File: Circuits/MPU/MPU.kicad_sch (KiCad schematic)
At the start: 12 parts, among them J1 5-1814400-1, J10 Conn_02x10_Odd_Even, J11 Conn_02x25_Odd_Even, J2 5-1814400-1, J3 DE9_Plug, J4 DE9_Plug, J5 0010085031, J6 DE9_Receptacle, J7 DE9_Receptacle, J8 Conn_02x05_Odd_Even, J9 Conn_02x13_Odd_Even, U1 ProASIC

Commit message: MXS interface
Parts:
- added J13: Pico-Lock-8, Connector_Molex:Molex_Pico-Lock_504050-0891_1x08-1MP_P1.50mm_Horizontal, symbol Connector_Generic:Conn_01x08
- J3, J4: value DE9_Plug -> MDM9_Plug
- J7: value DE9_Receptacle -> MDM9_Receptacle
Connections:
- net GND: now also J13.1 (Pin_1), J13.4 (Pin_4), J13.8 (Pin_8)
- new net Serial Interfaces/MXAD: J13.7 (Pin_7)
- new net Serial Interfaces/MXAS: J13.3 (Pin_3)
- new net Serial Interfaces/MXCLK: J13.5 (Pin_5)
- new net Serial Interfaces/MXDD: J13.6 (Pin_6)
- new net Serial Interfaces/MXDS: J13.2 (Pin_2)
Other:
- sheet Serial Interfaces ports: added MXAD, MXAS, MXCLK, MXDD, MXDS; removed none

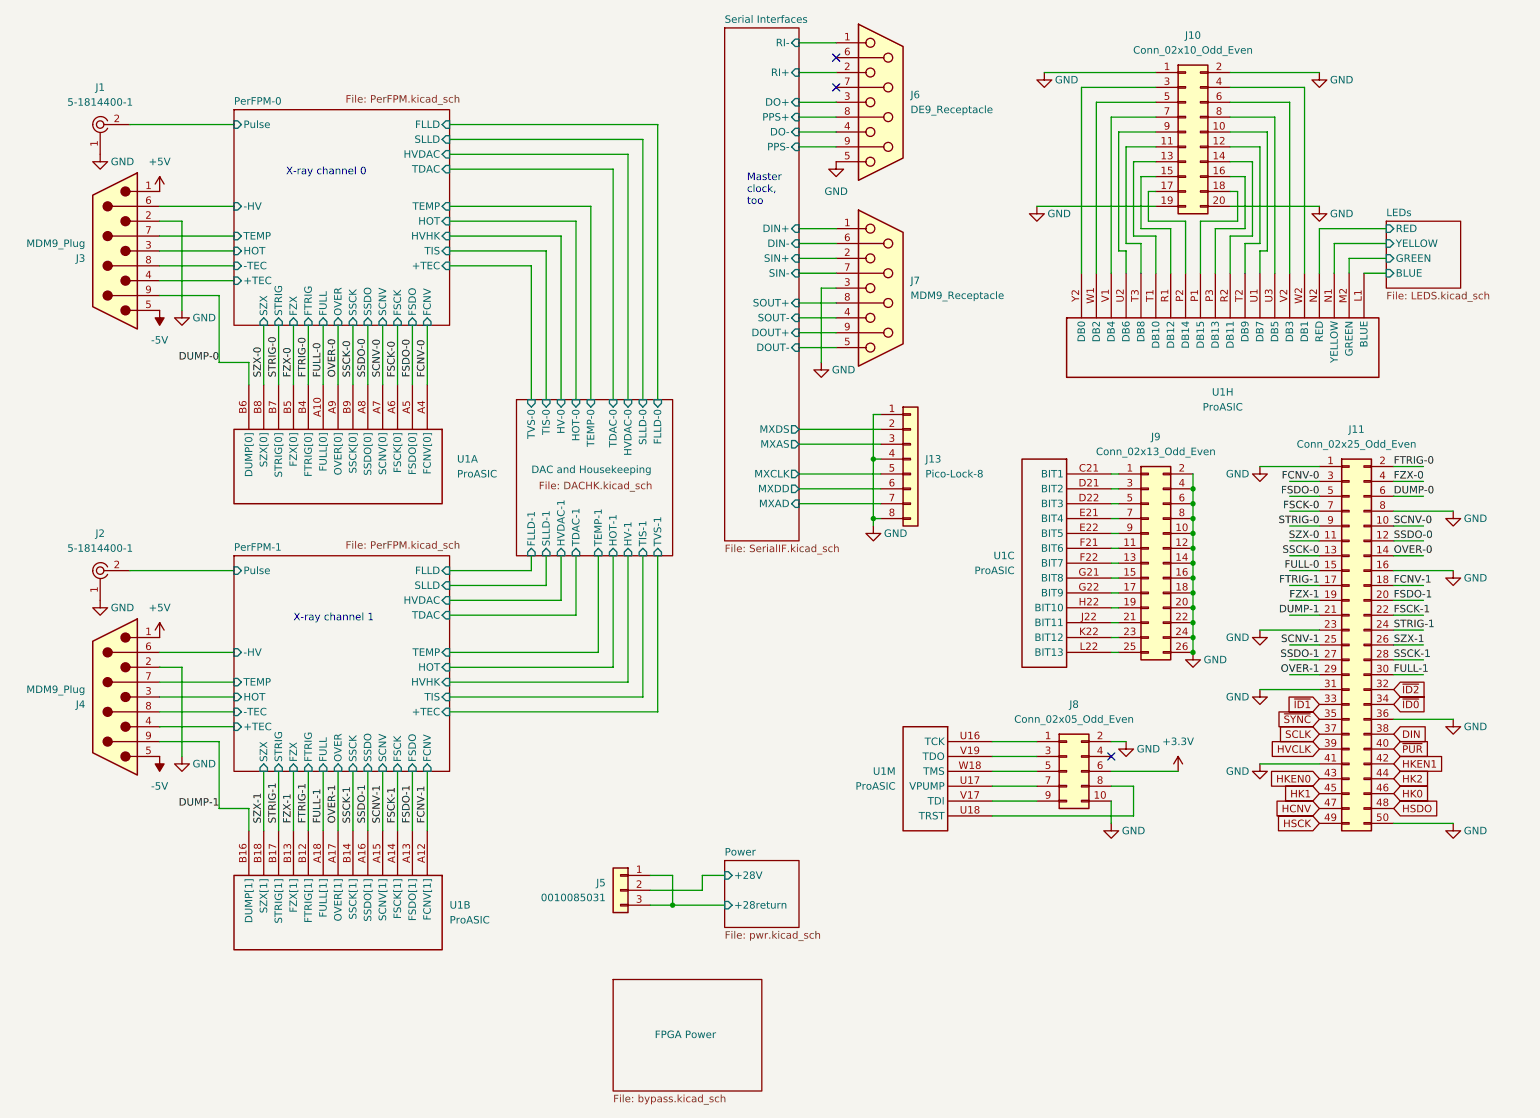
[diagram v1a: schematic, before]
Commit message: LVDS I/F for HV
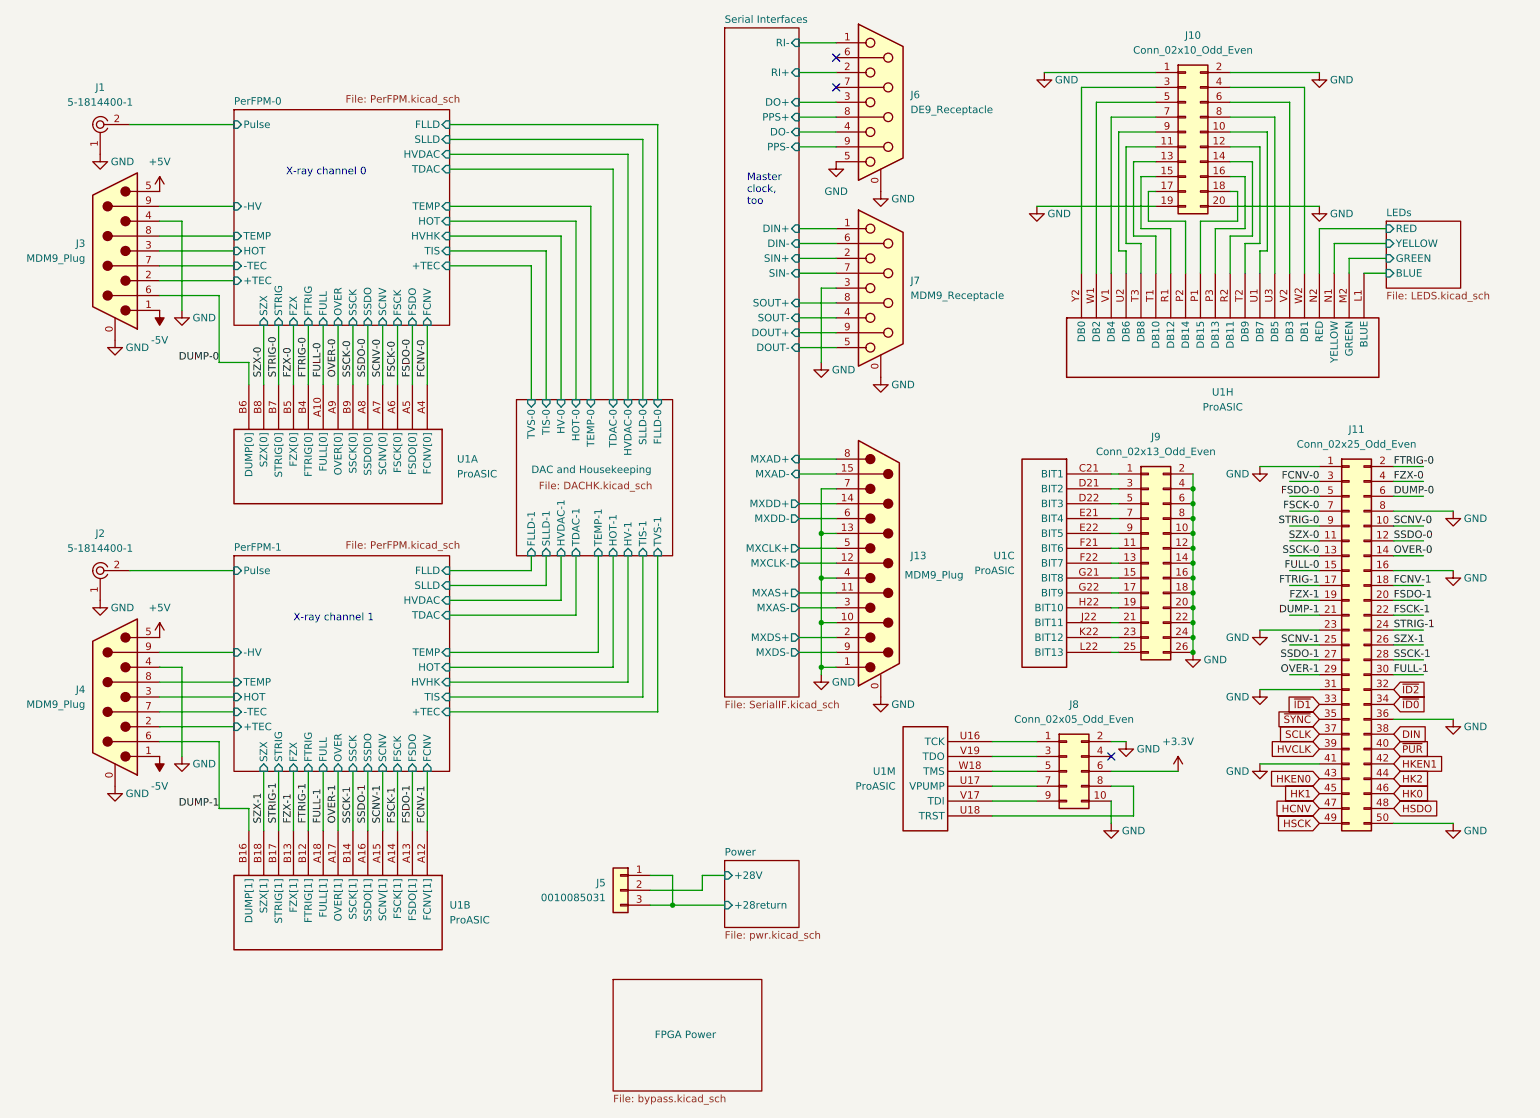
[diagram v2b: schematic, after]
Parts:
- removed J13: Pico-Lock-8, Connector_Molex:Molex_Pico-Lock_504050-0891_1x08-1MP_P1.50mm_Horizontal, symbol Connector_Generic:Conn_01x08
- removed J3, J4: MDM9_Plug, symbol Connector:DE9_Plug
- removed J6: DE9_Receptacle, symbol Connector:DE9_Receptacle
- removed J7: MDM9_Receptacle, symbol Connector:DE9_Receptacle
- added J13: MDM9_Plug, symbol Connector:DA15_Plug_MountingHoles
- added J3, J4: MDM9_Plug, symbol Connector:DE9_Plug_MountingHoles
- added J6: DE9_Receptacle, symbol Connector:DE9_Receptacle_MountingHoles
- added J7: MDM9_Receptacle, symbol Connector:DE9_Receptacle_MountingHoles
- U1: desc FPGA -> FPGA; manf# A3PE3000-FGG484 -> A3PE3000-FGG484
- U1: desc FPGA -> FPGA; manf# (none) -> A3PE3000-FGG484
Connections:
- net +5V: now also J3.5, J4.5
- net -5V: now also J3.1, J4.1
- net DUMP-0: now also J3.6
- net DUMP-1: now also J4.6
- net GND: now also J13.0 (PAD), J13.1, J13.10 (P10), J13.13 (P13), J13.4, J13.7, J3.0 (PAD), J3.4, J4.0 (PAD), J4.4, J6.0 (PAD), J6.5, J7.0 (PAD), J7.3
- net PerFPM-0/+TEC: now also J3.2
- net PerFPM-0/-HV: now also J3.9
- net PerFPM-0/-TEC: now also J3.7
- net PerFPM-0/HOT: now also J3.3
- net PerFPM-0/TEMP: now also J3.8
- net PerFPM-1/+TEC: now also J4.2
- net PerFPM-1/-HV: now also J4.9
- net PerFPM-1/-TEC: now also J4.7
- net PerFPM-1/HOT: now also J4.3
- net PerFPM-1/TEMP: now also J4.8
- net Serial Interfaces/DIN+: now also J7.1
- net Serial Interfaces/DIN-: now also J7.6
- net Serial Interfaces/DO+: now also J6.3
- net Serial Interfaces/DO-: now also J6.4
- net Serial Interfaces/DOUT+: now also J7.9
- net Serial Interfaces/DOUT-: now also J7.5
- net Serial Interfaces/PPS+: now also J6.8
- net Serial Interfaces/PPS-: now also J6.9
- net Serial Interfaces/RI+: now also J6.2
- net Serial Interfaces/RI-: now also J6.1
- net Serial Interfaces/SIN+: now also J7.2
- net Serial Interfaces/SIN-: now also J7.7
- net Serial Interfaces/SOUT+: now also J7.8
- net Serial Interfaces/SOUT-: now also J7.4
- new net Serial Interfaces/MXAD+: J13.8
- new net Serial Interfaces/MXAD-: J13.15 (P15)
- new net Serial Interfaces/MXAS+: J13.11 (P111)
- new net Serial Interfaces/MXAS-: J13.3
- new net Serial Interfaces/MXCLK+: J13.5
- new net Serial Interfaces/MXCLK-: J13.12 (P12)
- new net Serial Interfaces/MXDD+: J13.14 (P14)
- new net Serial Interfaces/MXDD-: J13.6
- new net Serial Interfaces/MXDS+: J13.2
- new net Serial Interfaces/MXDS-: J13.9 (P9)
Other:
- sheet Serial Interfaces ports: added MXAD+, MXAD-, MXAS+, MXAS-, MXCLK+, MXCLK-, MXDD+, MXDD-, MXDS+, MXDS-; removed MXAD, MXAS, MXCLK, MXDD, MXDS

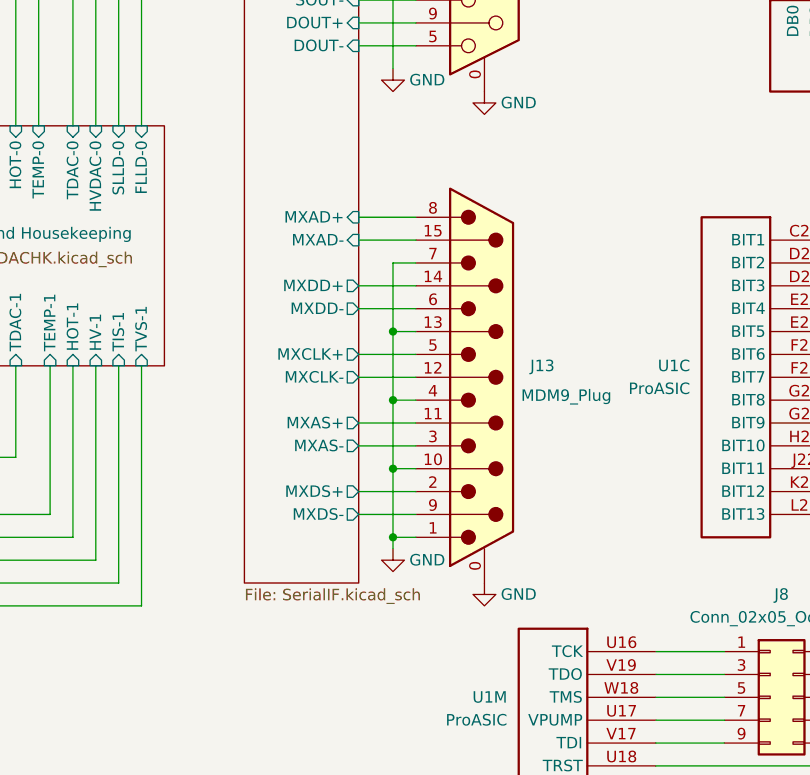
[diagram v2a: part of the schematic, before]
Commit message: PPS is RS422, add MXINH
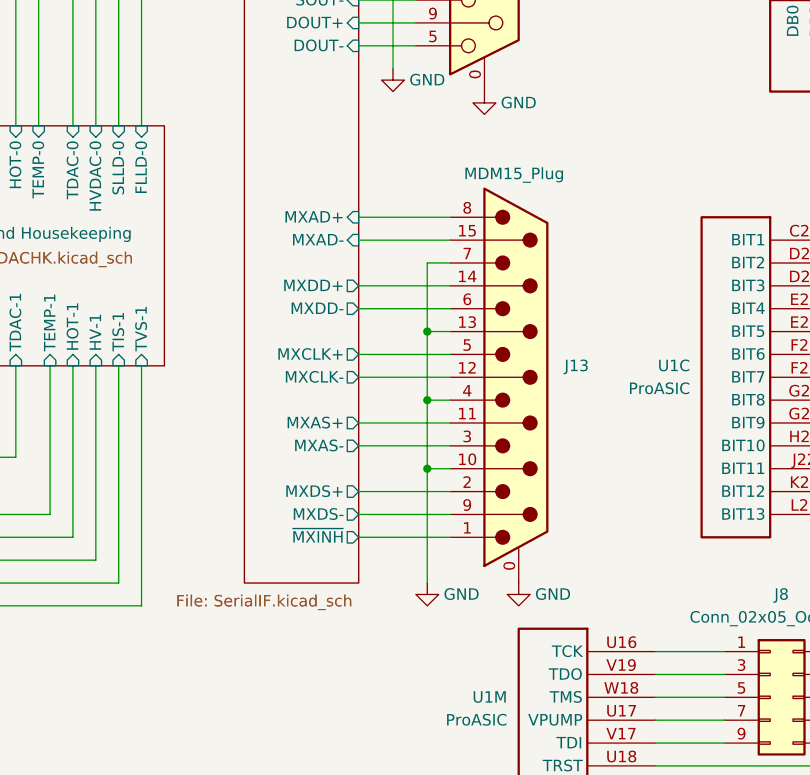
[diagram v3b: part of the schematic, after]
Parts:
- J13: value MDM9_Plug -> MDM15_Plug
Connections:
- net GND: no longer J13.1
- new net Serial Interfaces/~{MXINH}: J13.1
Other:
- sheet Serial Interfaces ports: added ~{MXINH}; removed none
- moved on the sheet: J13
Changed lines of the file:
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@@
 	(title_block
 		(title "QuERI MPU")
-		(date "2024-06-05")
-		(rev "RR1")
+		(date "2024-06-27")
+		(rev "RR3")
 		(company "Noqsi Aerospace Ltd")
 		(comment 1 "15 Blanchard Avenue, Billerica MA 01821")
@@
 	)
 	(junction
-		(at 151.13 110.49)
+		(at 154.94 110.49)
 		(diameter 0)
 		(color 0 0 0 0)
@@
 	)
 	(junction
-		(at 151.13 118.11)
+		(at 154.94 118.11)
 		(diameter 0)
 		(color 0 0 0 0)
@@
 	)
 	(junction
-		(at 151.13 102.87)
+		(at 154.94 102.87)
 		(diameter 0)
 		(color 0 0 0 0)
@@
 	)
 	(junction
-		(at 151.13 125.73)
-		(diameter 0)
-		(color 0 0 0 0)
-	)
-	(junction
 		(at 214.63 100.33)
 		(diameter 0)
@@
 	(wire
 		(pts
-			(xy 147.32 115.57) (xy 153.67 115.57)
+			(xy 147.32 115.57) (xy 157.48 115.57)
 		)
 		(stroke
@@
 	(wire
 		(pts
-			(xy 151.13 102.87) (xy 153.67 102.87)
+			(xy 154.94 102.87) (xy 157.48 102.87)
 		)
 		(stroke
@@
 	(wire
 		(pts
-			(xy 151.13 118.11) (xy 153.67 118.11)
+			(xy 154.94 118.11) (xy 157.48 118.11)
 		)
 		(stroke
@@
 	(wire
 		(pts
-			(xy 151.13 95.25) (xy 153.67 95.25)
+			(xy 154.94 95.25) (xy 157.48 95.25)
 		)
 		(stroke
@@
 	(wire
 		(pts
-			(xy 151.13 125.73) (xy 151.13 118.11)
+			(xy 154.94 118.11) (xy 154.94 130.81)
 		)
 		(stroke
@@
 	(wire
 		(pts
-			(xy 151.13 102.87) (xy 151.13 95.25)
+			(xy 154.94 102.87) (xy 154.94 95.25)
 		)
 		(stroke
@@
 	(wire
 		(pts
-			(xy 147.32 92.71) (xy 153.67 92.71)
+			(xy 147.32 92.71) (xy 157.48 92.71)
 		)
 		(stroke
@@
 	(wire
 		(pts
-			(xy 147.32 107.95) (xy 153.67 107.95)
+			(xy 147.32 107.95) (xy 157.48 107.95)
 		)
 		(stroke
@@
 	(wire
 		(pts
-			(xy 147.32 123.19) (xy 153.67 123.19)
+			(xy 147.32 123.19) (xy 157.48 123.19)
 		)
 		(stroke
@@
 	(wire
 		(pts
-			(xy 151.13 127) (xy 151.13 125.73)
-		)
-		(stroke
-			(width 0)
-			(type default)
-		)
-	)
-	(wire
-		(pts
 			(xy 87.63 114.3) (xy 106.68 114.3)
 		)
@@
 	(wire
 		(pts
-			(xy 147.32 120.65) (xy 153.67 120.65)
+			(xy 147.32 120.65) (xy 157.48 120.65)
 		)
 		(stroke
@@
 	(wire
 		(pts
-			(xy 147.32 100.33) (xy 153.67 100.33)
+			(xy 147.32 100.33) (xy 157.48 100.33)
 		)
 		(stroke
@@
 	(wire
 		(pts
-			(xy 147.32 97.79) (xy 153.67 97.79)
+			(xy 147.32 97.79) (xy 157.48 97.79)
 		)
 		(stroke
@@
 	(wire
 		(pts
-			(xy 151.13 110.49) (xy 153.67 110.49)
+			(xy 154.94 110.49) (xy 157.48 110.49)
 		)
 		(stroke
@@
 	(wire
 		(pts
-			(xy 151.13 125.73) (xy 153.67 125.73)
-		)
-		(stroke
-			(width 0)
-			(type default)
-		)
-	)
-	(wire
-		(pts
 			(xy 204.47 151.13) (xy 204.47 146.05)
 		)
@@
 	(wire
 		(pts
-			(xy 151.13 110.49) (xy 151.13 102.87)
+			(xy 154.94 110.49) (xy 154.94 102.87)
 		)
 		(stroke
@@
 	(wire
 		(pts
-			(xy 147.32 105.41) (xy 153.67 105.41)
+			(xy 147.32 105.41) (xy 157.48 105.41)
 		)
 		(stroke
@@
 	(wire
 		(pts
-			(xy 147.32 90.17) (xy 153.67 90.17)
+			(xy 147.32 90.17) (xy 157.48 90.17)
 		)
 		(stroke
@@
 	(wire
 		(pts
-			(xy 147.32 113.03) (xy 153.67 113.03)
+			(xy 147.32 113.03) (xy 157.48 113.03)
 		)
 		(stroke
@@
 	(wire
 		(pts
-			(xy 151.13 118.11) (xy 151.13 110.49)
+			(xy 154.94 118.11) (xy 154.94 110.49)
 		)
 		(stroke
@@
 	(wire
 		(pts
+			(xy 147.32 125.73) (xy 157.48 125.73)
+		)
+		(stroke
+			(width 0)
+			(type default)
+		)
+	)
+	(wire
+		(pts
 			(xy 214.63 107.95) (xy 214.63 110.49)
 		)
@@
 		(pin "M16"
 		)
-		(pin "M19"
-		)
-		(pin "M20"
+		(pin "M3"
 		)
 		(pin "M21"
@@
 		(pin "W21"
 		)
+		(pin "M7"
+		)
 		(instances
 			(project "MPU"
@@
 	(symbol
 		(lib_id "power:GND")
-		(at 161.29 130.81 0)
+		(at 165.1 130.81 0)
 		(unit 1)
 		(exclude_from_sim no)
@@
 		(dnp no)
 		(property "Reference" "#PWR09"
-			(at 161.29 137.16 0)
+			(at 165.1 137.16 0)
 			(effects
 				(font
@@
 		)
 		(property "Value" "GND"
-			(at 165.1 132.08 0)
+			(at 168.91 132.08 0)
 			(effects
 				(font
@@
 		)
 		(property "Footprint" ""
-			(at 161.29 130.81 0)
+			(at 165.1 130.81 0)
 			(effects
 				(font
@@
 		)
 		(property "Datasheet" ""
-			(at 161.29 130.81 0)
+			(at 165.1 130.81 0)
 			(effects
 				(font
@@
 		)
 		(property "Description" "Power symbol creates a global label with name \"GND\" , ground"
-			(at 161.29 130.81 0)
+			(at 165.1 130.81 0)
 			(effects
 				(font
@@
 		(pin "AA1"
 		)
-		(pin "M19"
-		)
-		(pin "M20"
+		(pin "M3"
 		)
 		(pin "M21"
@@
 		(pin "W21"
 		)
+		(pin "M7"
+		)
 		(instances
 			(project "MPU"
@@
 		(pin "M16"
 		)
-		(pin "M19"
-		)
-		(pin "M20"
+		(pin "M3"
 		)
 		(pin "M21"
@@
 		(pin "W21"
 		)
+		(pin "M7"
+		)
 		(instances
 			(project "MPU"
@@
 		(pin "M16"
 		)
-		(pin "M19"
-		)
-		(pin "M20"
+		(pin "M3"
 		)
 		(pin "M21"
@@
 		(pin "W21"
 		)
+		(pin "M7"
+		)
 		(instances
 			(project "MPU"
@@
 	(symbol
 		(lib_id "Connector:DA15_Plug_MountingHoles")
-		(at 161.29 107.95 0)
+		(at 165.1 107.95 0)
 		(unit 1)
 		(exclude_from_sim no)
@@
 		(dnp no)
 		(property "Reference" "J13"
-			(at 166.37 106.6799 0)
+			(at 170.18 106.6799 0)
 			(effects
 				(font
@@
 			)
 		)
-		(property "Value" "MDM9_Plug"
-			(at 165.354 109.982 0)
+		(property "Value" "MDM15_Plug"
+			(at 159.004 85.344 0)
 			(effects
 				(font
@@
 		)
 		(property "Footprint" ""
-			(at 161.29 107.95 0)
+			(at 165.1 107.95 0)
 			(effects
 				(font
@@
 		)
 		(property "Datasheet" "~"
-			(at 161.29 107.95 0)
+			(at 165.1 107.95 0)
 			(effects
 				(font
@@
 		)
 		(property "Description" "15-pin male plug pin D-SUB connector (low-density/2 columns), Mounting Hole"
-			(at 161.29 107.95 0)
+			(at 165.1 107.95 0)
 			(effects
 				(font
@@
 	(symbol
 		(lib_id "power:GND")
-		(at 151.13 127 0)
+		(at 154.94 130.81 0)
 		(unit 1)
 		(exclude_from_sim no)
@@
 		(dnp no)
 		(property "Reference" "#PWR010"
-			(at 151.13 133.35 0)
+			(at 154.94 137.16 0)
 			(effects
 				(font
@@
 		)
 		(property "Value" "GND"
-			(at 154.94 128.27 0)
+			(at 158.75 132.08 0)
 			(effects
 				(font
@@
 		)
 		(property "Footprint" ""
-			(at 151.13 127 0)
+			(at 154.94 130.81 0)
 			(effects
 				(font
@@
 		)
 		(property "Datasheet" ""
-			(at 151.13 127 0)
+			(at 154.94 130.81 0)
 			(effects
 				(font
@@
 		)
 		(property "Description" "Power symbol creates a global label with name \"GND\" , ground"
-			(at 151.13 127 0)
+			(at 154.94 130.81 0)
 			(effects
 				(font
@@
 	)
 	(symbol
+		(lib_name "5-1814400-1_1")
 		(lib_id "dk_Coax:5-1814400-1")
 		(at 27.94 33.02 0)
@@
 		(pin "M16"
 		)
-		(pin "M19"
-		)
-		(pin "M20"
+		(pin "M3"
 		)
 		(pin "M21"
@@
 		(pin "W21"
 		)
+		(pin "M7"
+		)
 		(instances
 			(project "MPU"
@@
 		(at 134.62 16.51)
 		(size 12.7 114.3)
-		(fields_autoplaced yes)
 		(stroke
 			(width 0.1524)
@@
 		)
 		(property "Sheetfile" "SerialIF.kicad_sch"
-			(at 134.62 131.3946 0)
+			(at 127 132.08 0)
 			(effects
 				(font
@@
 			(effects
 				(font
+					(size 1.27 1.27)
+				)
+				(justify right)
+			)
+		)
+		(pin "~{MXINH}" output
+			(at 147.32 125.73 0)
+			(effects
+				(font
